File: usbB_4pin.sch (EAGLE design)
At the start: 13 parts, among them IC1 788TV, IC2 TINY13-20PU, X1 PN61729-S

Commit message: minor layout changes
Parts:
- removed JP1: (no value), pinhead:PINHD-2X3
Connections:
- removed net N$10: IC2.PB1/PCINT1/AIN1/OC0B/INT0/MISO, LED1-1.A
- removed net N$11: IC2.PB3/PCINT3/CLKI/ADC3, LED1-2.A
- new net N$3: IC2.PB3/PCINT3/CLKI/ADC3, LED1-1.A
- new net N$5: IC2.PB1/PCINT1/AIN1/OC0B/INT0/MISO, LED1-2.A
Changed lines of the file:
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@@
 <part name="SV1" library="con-lstb" deviceset="MA04-1" device=""/>
 <part name="X1" library="con-berg" deviceset="PN61729-S" device=""/>
-<part name="JP1" library="pinhead" deviceset="PINHD-2X3" device=""/>
 </parts>
 <sheets>
@@
 <instance part="SV1" gate="1" x="73.66" y="10.16" rot="R90"/>
 <instance part="X1" gate="G$1" x="-7.62" y="68.58" rot="R180"/>
-<instance part="JP1" gate="A" x="91.44" y="12.7"/>
 </instances>
 <busses>
@@
 </segment>
 </net>
-<net name="N$9" class="0">
-<segment>
-<pinref part="IC2" gate="G$1" pin="PB4/PCINT4/ADC2"/>
-<pinref part="LED1" gate="-3" pin="A"/>
-<wire x1="53.34" y1="35.56" x2="109.22" y2="35.56" width="0.1524" layer="91"/>
-<wire x1="109.22" y1="35.56" x2="109.22" y2="30.48" width="0.1524" layer="91"/>
-</segment>
-</net>
-<net name="N$10" class="0">
-<segment>
-<pinref part="IC2" gate="G$1" pin="PB1/PCINT1/AIN1/OC0B/INT0/MISO"/>
-<wire x1="53.34" y1="43.18" x2="104.14" y2="43.18" width="0.1524" layer="91"/>
-<wire x1="104.14" y1="43.18" x2="104.14" y2="50.8" width="0.1524" layer="91"/>
-<pinref part="LED1" gate="-1" pin="A"/>
-<wire x1="104.14" y1="50.8" x2="109.22" y2="50.8" width="0.1524" layer="91"/>
-</segment>
-</net>
-<net name="N$11" class="0">
-<segment>
-<pinref part="IC2" gate="G$1" pin="PB3/PCINT3/CLKI/ADC3"/>
-<pinref part="LED1" gate="-2" pin="A"/>
-<wire x1="53.34" y1="38.1" x2="109.22" y2="38.1" width="0.1524" layer="91"/>
-<wire x1="109.22" y1="38.1" x2="109.22" y2="40.64" width="0.1524" layer="91"/>
-</segment>
-</net>
 <net name="N$12" class="0">
 <segment>
@@
 </segment>
 </net>
+<net name="N$3" class="0">
+<segment>
+<pinref part="IC2" gate="G$1" pin="PB3/PCINT3/CLKI/ADC3"/>
+<wire x1="53.34" y1="38.1" x2="88.9" y2="38.1" width="0.1524" layer="91"/>
+<wire x1="88.9" y1="38.1" x2="88.9" y2="50.8" width="0.1524" layer="91"/>
+<pinref part="LED1" gate="-1" pin="A"/>
+<wire x1="88.9" y1="50.8" x2="109.22" y2="50.8" width="0.1524" layer="91"/>
+</segment>
+</net>
+<net name="N$5" class="0">
+<segment>
+<pinref part="IC2" gate="G$1" pin="PB1/PCINT1/AIN1/OC0B/INT0/MISO"/>
+<pinref part="LED1" gate="-2" pin="A"/>
+<wire x1="53.34" y1="43.18" x2="109.22" y2="43.18" width="0.1524" layer="91"/>
+<wire x1="109.22" y1="43.18" x2="109.22" y2="40.64" width="0.1524" layer="91"/>
+</segment>
+</net>
+<net name="N$9" class="0">
+<segment>
+<pinref part="IC2" gate="G$1" pin="PB4/PCINT4/ADC2"/>
+<pinref part="LED1" gate="-3" pin="A"/>
+<wire x1="53.34" y1="35.56" x2="109.22" y2="35.56" width="0.1524" layer="91"/>
+<wire x1="109.22" y1="35.56" x2="109.22" y2="30.48" width="0.1524" layer="91"/>
+</segment>
+</net>

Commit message: correct values
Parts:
- C1: value 22µF -> 33u
- C2: value 100nF -> 470n
- C3: value 100nF -> 100n
- R1: value (none) -> 10k
- R2: value 150Ohm -> 150
- R3, R4: value 91Ohm -> 91
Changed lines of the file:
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@@
 </classes>
 <parts>
-<part name="C1" library="rcl" deviceset="CPOL-EU" device="E2,5-6E" value="22µF"/>
-<part name="C2" library="rcl" deviceset="C-EU" device="050-025X075" value="100nF"/>
-<part name="C3" library="rcl" deviceset="C-EU" device="050-025X075" value="100nF"/>
-<part name="R1" library="resistor" deviceset="R-EU_" device="0204/7"/>
-<part name="R2" library="resistor" deviceset="R-EU_" device="0204/7" value="150Ohm"/>
-<part name="R3" library="resistor" deviceset="R-EU_" device="0204/7" value="91Ohm"/>
-<part name="R4" library="resistor" deviceset="R-EU_" device="0204/7" value="91Ohm"/>
+<part name="C1" library="rcl" deviceset="CPOL-EU" device="E2,5-6E" value="33u"/>
+<part name="C2" library="rcl" deviceset="C-EU" device="050-025X075" value="470n"/>
+<part name="C3" library="rcl" deviceset="C-EU" device="050-025X075" value="100n"/>
+<part name="R1" library="resistor" deviceset="R-EU_" device="0204/7" value="10k"/>
+<part name="R2" library="resistor" deviceset="R-EU_" device="0204/7" value="150"/>
+<part name="R3" library="resistor" deviceset="R-EU_" device="0204/7" value="91"/>
+<part name="R4" library="resistor" deviceset="R-EU_" device="0204/7" value="91"/>
 <part name="IC1" library="linear" deviceset="78*" device="TV" technology="8"/>
 <part name="IC2" library="atmel" deviceset="TINY13" device="PU" technology="-20"/>

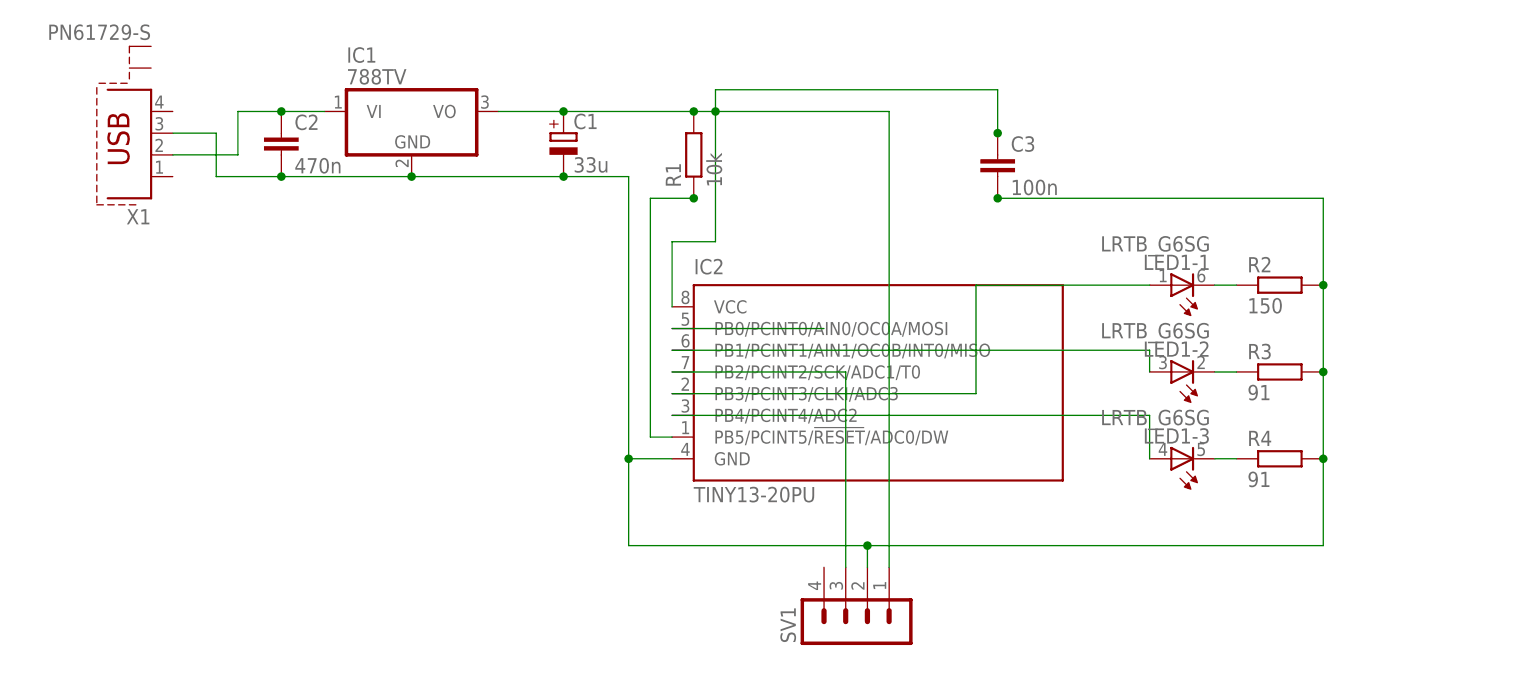
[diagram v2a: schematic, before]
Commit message: correct pin headers ftw
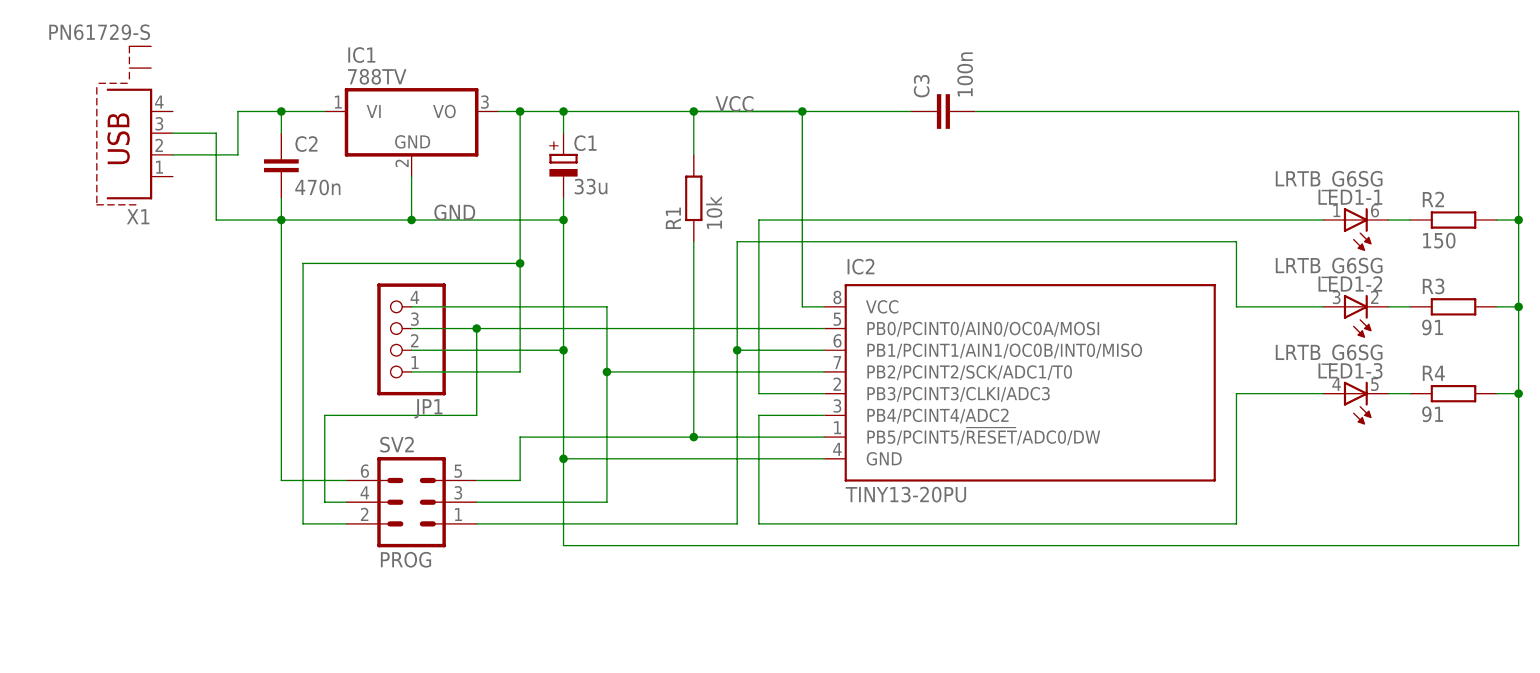
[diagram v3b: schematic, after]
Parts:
- removed SV1: (no value), con-lstb:MA04-1
- added JP1: (no value), pinhead:PINHD-1X4
- added SV2: PROG, con-ml:ML6
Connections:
- removed net N$12: IC2.PB0/PCINT0/AIN0/OC0A/MOSI
- removed net N$13: IC2.PB2/PCINT2/SCK/ADC1/T0, SV1.3
- removed net N$4: IC2.PB5/PCINT5/!RESET!/ADC0/DW, R1.1
- removed net N$5: IC2.PB1/PCINT1/AIN1/OC0B/INT0/MISO, LED1-2.A
- new net MISO: IC2.PB1/PCINT1/AIN1/OC0B/INT0/MISO, LED1-2.A, SV2.1
- new net N$10: IC2.PB0/PCINT0/AIN0/OC0A/MOSI, JP1.3, SV2.4
- new net SCK: IC2.PB2/PCINT2/SCK/ADC1/T0, JP1.4, SV2.3
- new net _RESET: IC2.PB5/PCINT5/!RESET!/ADC0/DW, R1.1, SV2.5
- net GND: now also JP1.2, SV2.6; no longer SV1.2
- net VCC: now also JP1.1, SV2.2; no longer SV1.1
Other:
- moved on the sheet: C1, C2, C3, IC2, LED1-1, LED1-2, LED1-3, R1, R2, R3, R4
